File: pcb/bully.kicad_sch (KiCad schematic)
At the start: 29 parts, among them J1 SM04B-SRSS-TB(LF)(SN), J2 Conn_01x04, U1 W25Q128JVS, U3 RP2040, U4 XC6206PxxxMR-Regulator_Linear, Y1 12MHz

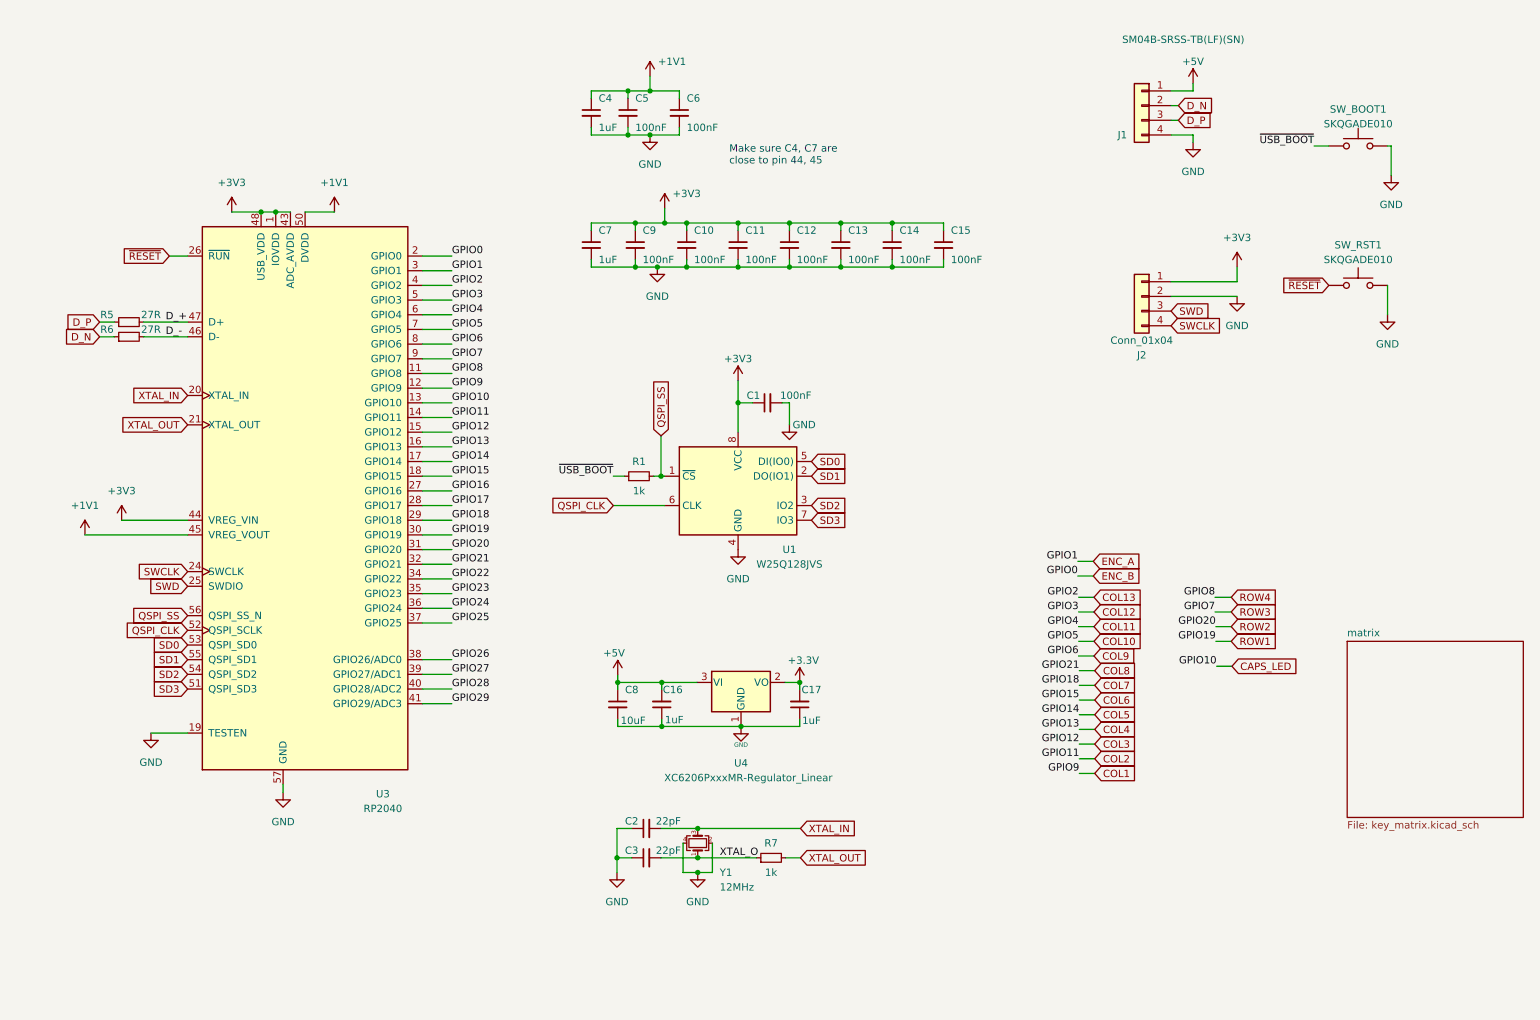
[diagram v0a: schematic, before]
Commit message: cleaned up schematic and added alps support
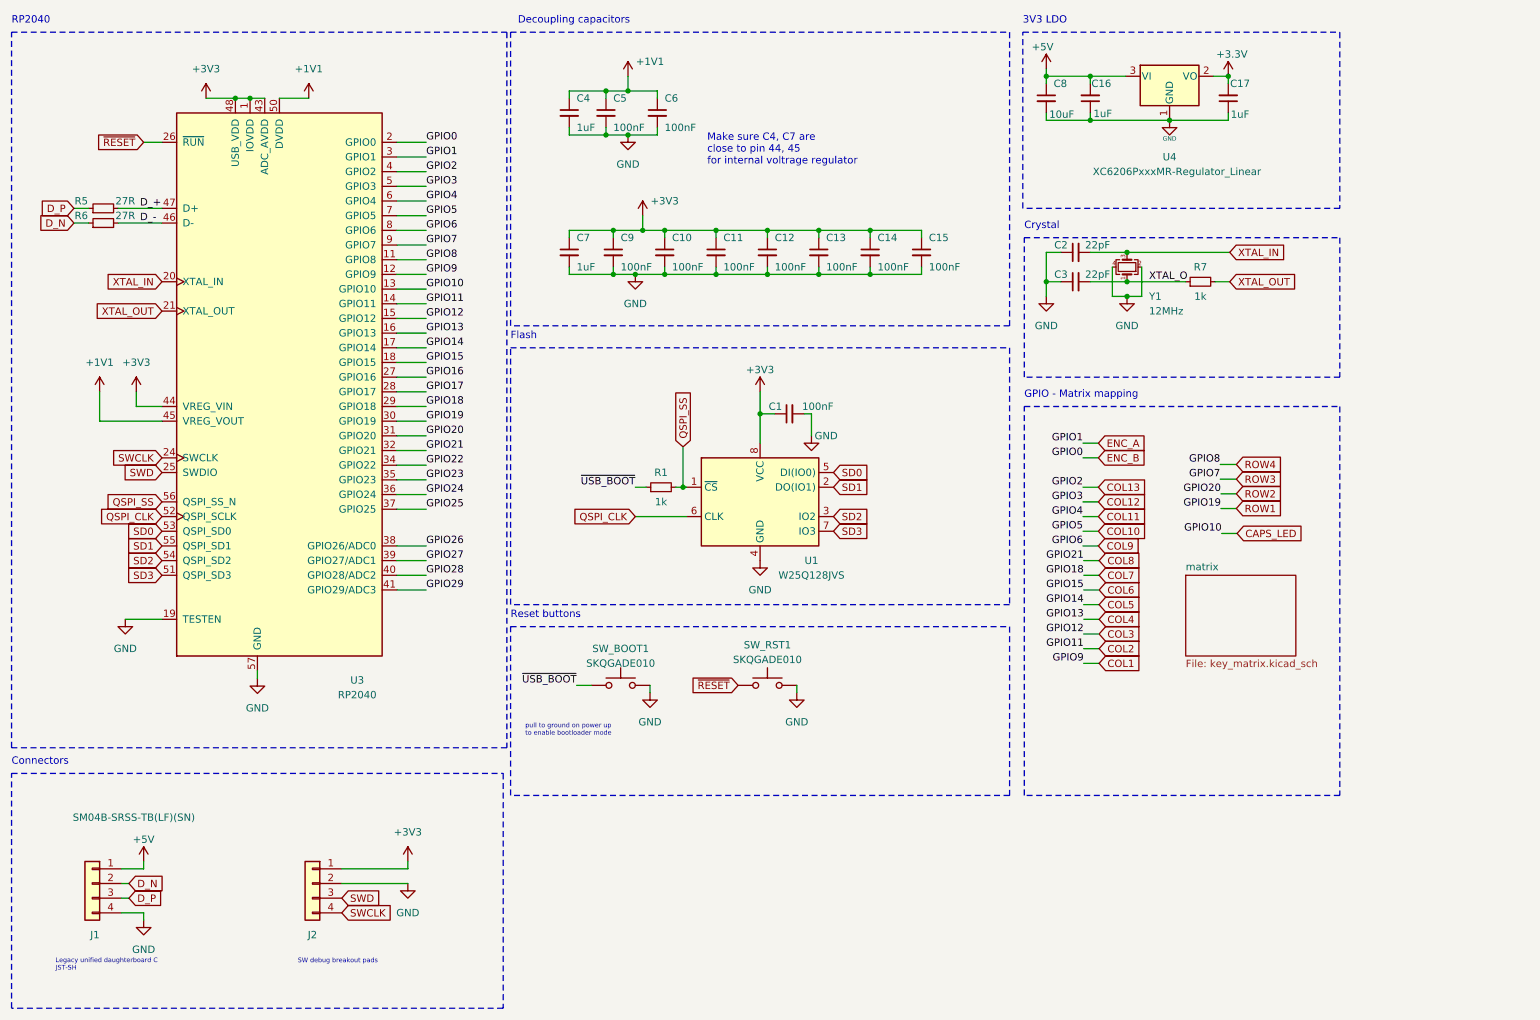
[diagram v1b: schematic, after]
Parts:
- C1, C10, C11, C12, C13, C14, C15, C5, C6, C9: LCSC C1525 -> (none)
- C16, C17, C4, C8: LCSC C52923 -> (none)
- C2, C3: LCSC C1555 -> (none)
- C7: LCSC C15525 -> (none)
- R1, R7: LCSC C11702 -> (none)
- R5, R6: LCSC C25190 -> (none)
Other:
- note added: "3V3 LDO"
- note added: "Connectors"
- note added: "Crystal"
- note added: "Decoupling capacitors"
- note added: "Flash"
- note added: "GPIO - Matrix mapping"
- note added: "Legacy unified daughterboard C JST-SH"
- note added: "Make sure C4, C7 are close to pin 44, 45 for internal voltrage regulator"
- note added: "RP2040"
- note added: "Reset buttons"
- note added: "SW debug breakout pads"
- note added: "pull to ground on power up to enable bootloader mode"
- note removed: "Make sure C4, C7 are close to pin 44, 45"
- company: Sleepdealer -> sporkus
- title: RP2040 - Design Guide -> Bully2040 - MX/Alps
- moved on the sheet: C1, C10, C11, C12, C13, C14, C15, C16, C17, C2, C3, C4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
